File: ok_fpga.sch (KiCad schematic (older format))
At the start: 39 parts, among them J12 Conn_Coaxial, J13 QWIIC_CONNECTOR-1MM, J14 Conn_Coaxial, J22 Conn_02x10_Counter_Clockwise, J23 Conn_02x10_Counter_Clockwise, U15 PCA9306, U16 NLSX3018DTR2G, U18 TXS0108EPW, U20 TXS0108EPW, U24 TCA9555, U25 TCA9555

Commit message: moved DCO 7960 signals to dedicated input clock routes
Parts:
- J12, J14: footprint (none) -> covg-kicad:BU-SMA-G; Manf# (none) -> WM26450
- J23: symbol Connector_Generic:Conn_02x05_Counter_Clockwise -> Connector_Generic:Conn_02x05_Odd_Even
- gave numbers to parts that had none: 18
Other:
- note added: "11 is a clock in"
- note added: "12 is a clock in"
- note added: "13 is a clock in"
- note added: "14 is a clock in"
- note removed: "Do a check of skew matching between DCO and D \nfor high-speed ADC"
- moved on the sheet: U24, U25

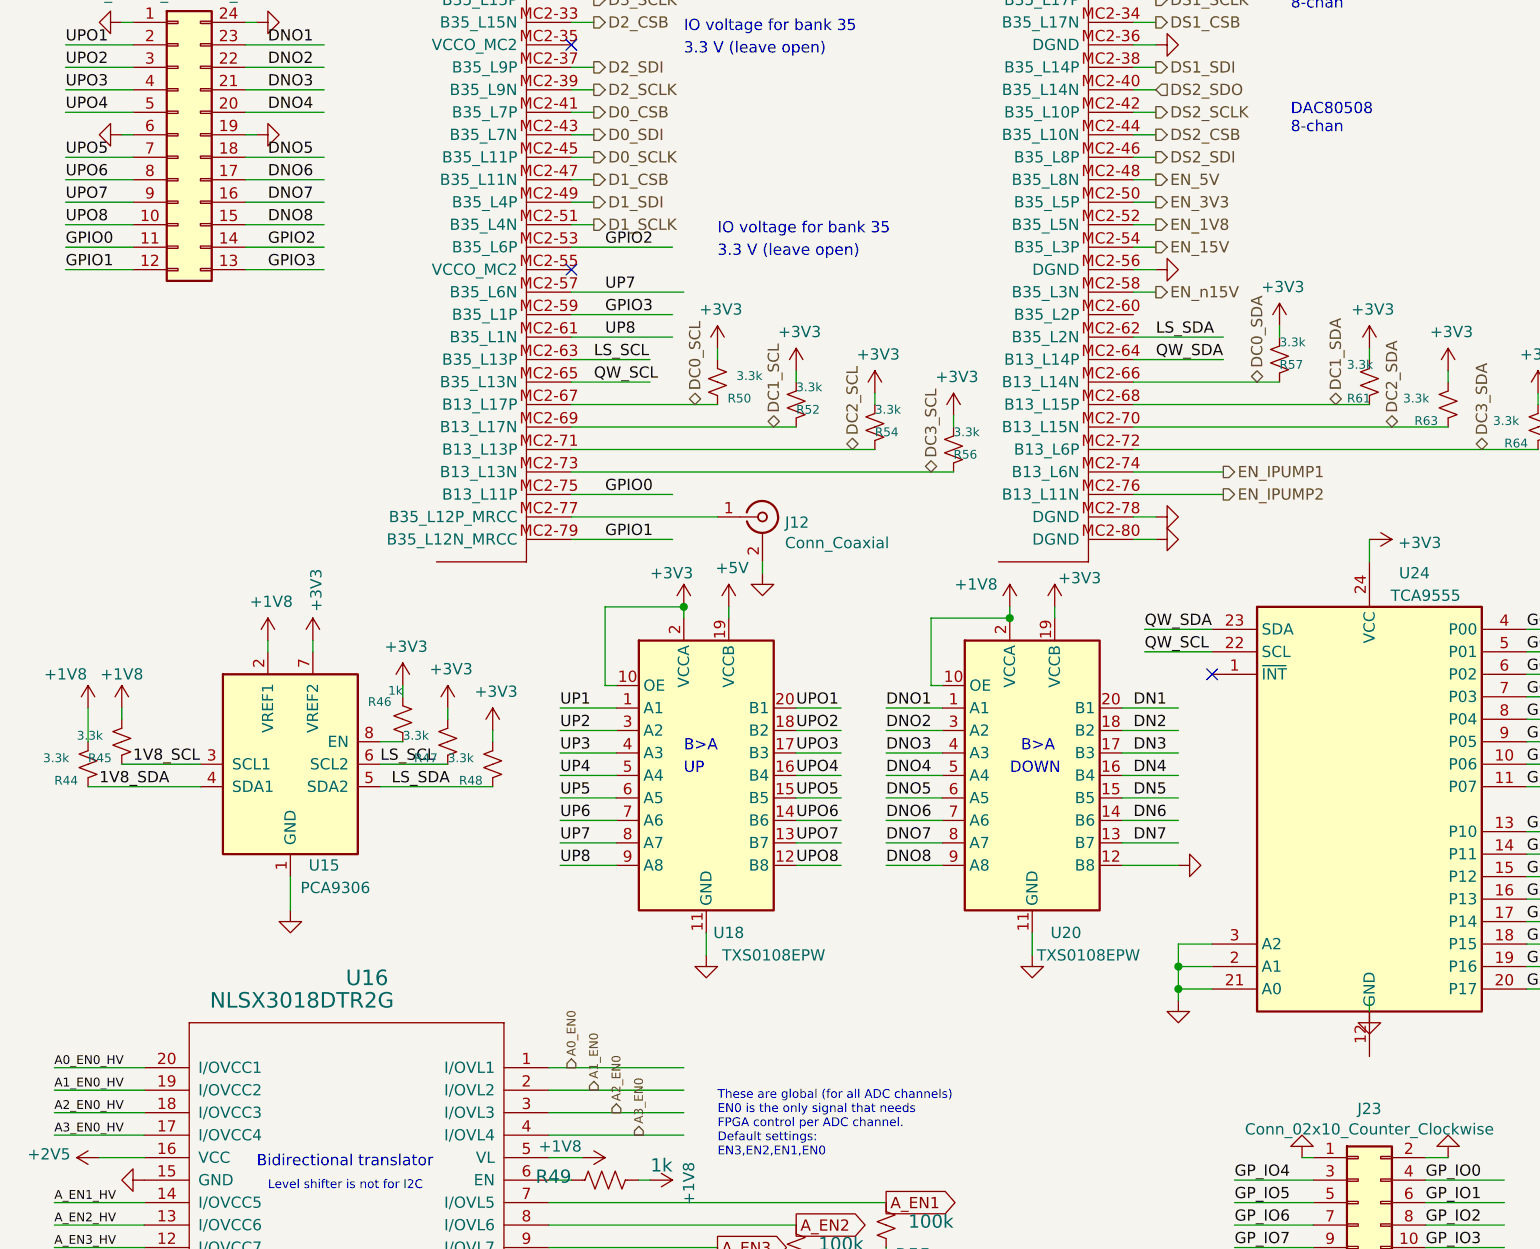
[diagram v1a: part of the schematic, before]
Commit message: added Unique ID chip
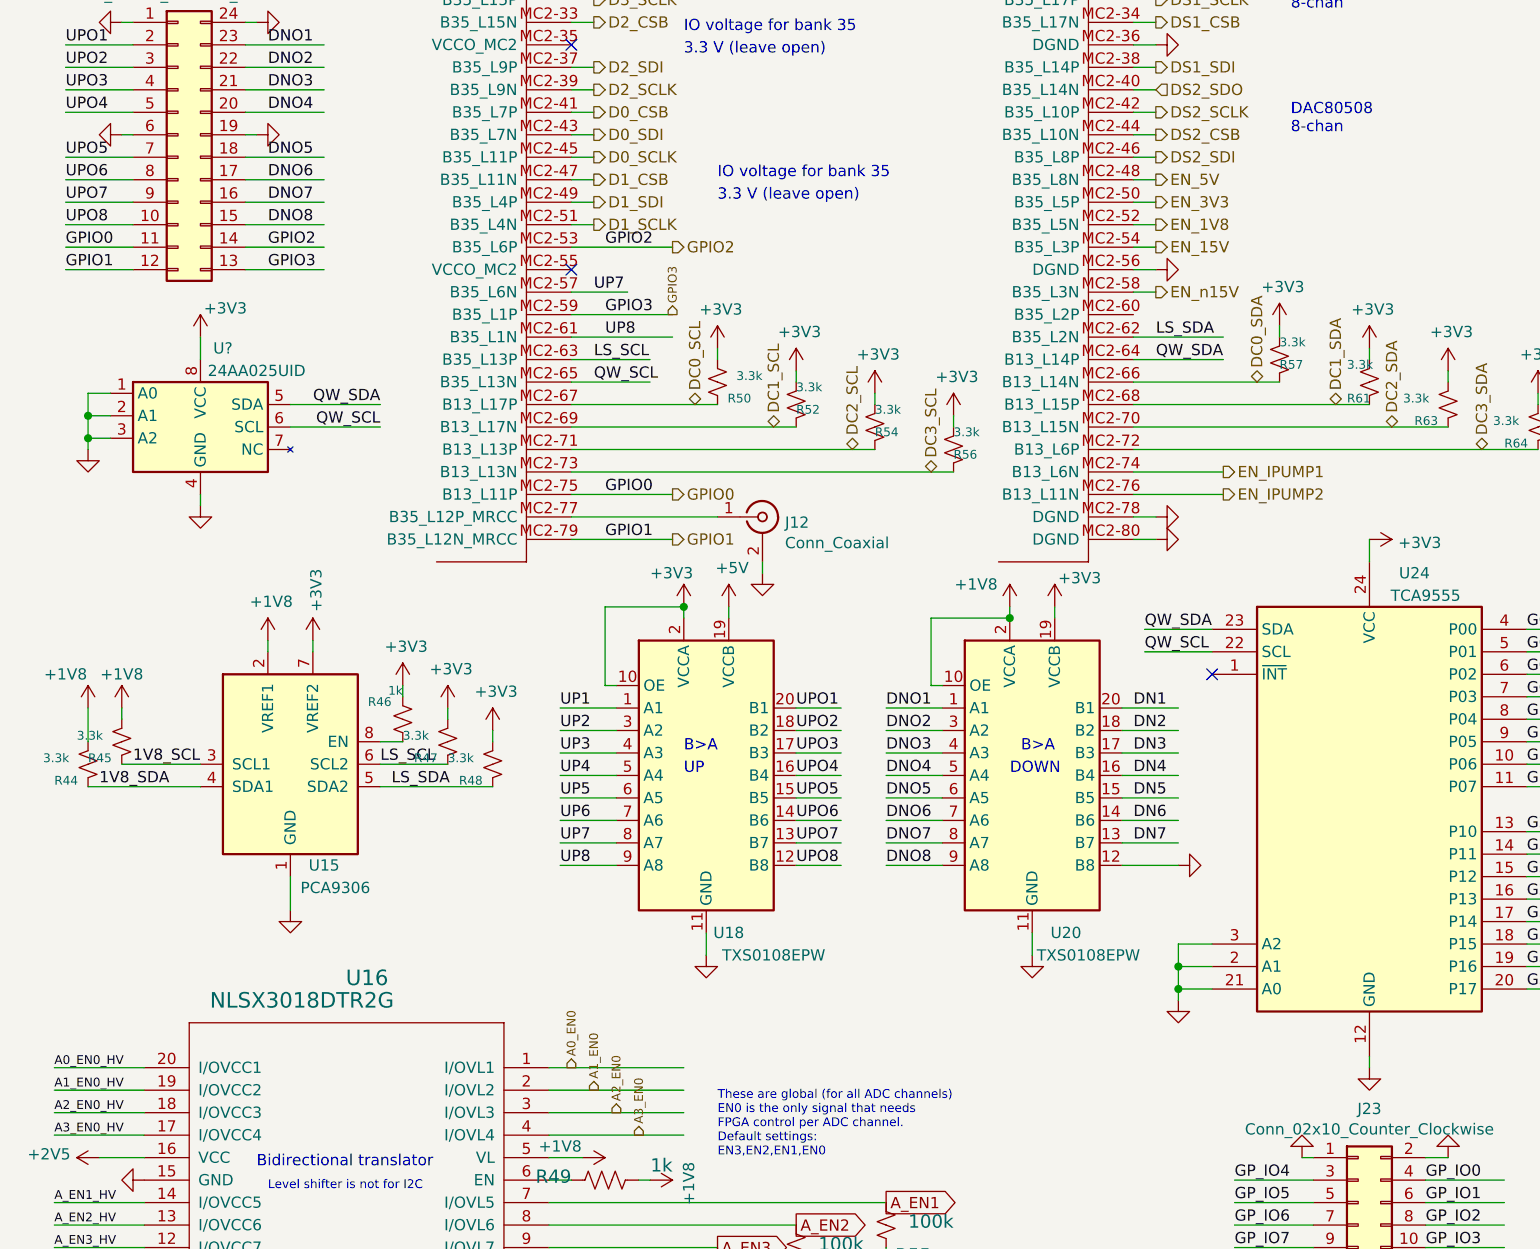
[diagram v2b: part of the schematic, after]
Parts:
- added U?: 24AA025UID, Package_SO:SOIC-8_3.9x4.9mm_P1.27mm, symbol covg-kicad:24AA025UID
- OK1: footprint covg-kicad:OPALKELLY_XEM6010 -> covg-kicad:OPALKELLY_XEM7310
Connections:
- wire segments 344 -> 354
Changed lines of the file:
@@
 F 0 "OK1" H 2700 4610 70  0000 R BNN
 F 1 "OPALKELLY_XEM6310" H 2500 2600 50  0001 C CNN
-F 2 "covg-kicad:OPALKELLY_XEM6010" H 2500 2600 50  0001 C CNN
+F 2 "covg-kicad:OPALKELLY_XEM7310" H 2500 2600 50  0001 C CNN
 F 3 "" H 2500 2600 50  0001 C CNN
 F 4 "BTE-040-02-F-D-A" H 2700 4710 50  0001 C CNN "Manf#"
@@
 F 0 "OK1" H 8000 4610 70  0000 R BNN
 F 1 "OPALKELLY_XEM6310" H 7800 2600 50  0001 C CNN
-F 2 "covg-kicad:OPALKELLY_XEM6010" H 7800 2600 50  0001 C CNN
+F 2 "covg-kicad:OPALKELLY_XEM7310" H 7800 2600 50  0001 C CNN
 F 3 "" H 7800 2600 50  0001 C CNN
 F 4 "BTE-040-02-F-D-A" H 8000 4710 50  0001 C CNN "Manf#"
@@
 F 0 "OK1" H 10700 4610 70  0000 R BNN
 F 1 "OPALKELLY_XEM6310" H 10500 2600 50  0001 C CNN
-F 2 "covg-kicad:OPALKELLY_XEM6010" H 10500 2600 50  0001 C CNN
+F 2 "covg-kicad:OPALKELLY_XEM7310" H 10500 2600 50  0001 C CNN
 F 3 "" H 10500 2600 50  0001 C CNN
 F 4 "BTE-040-02-F-D-A" H 10700 4710 50  0001 C CNN "Manf#"
@@
 F 0 "OK1" H 5200 4610 70  0000 R BNN
 F 1 "OPALKELLY_XEM6310" H 5000 2600 50  0001 C CNN
-F 2 "covg-kicad:OPALKELLY_XEM6010" H 5000 2600 50  0001 C CNN
+F 2 "covg-kicad:OPALKELLY_XEM7310" H 5000 2600 50  0001 C CNN
 F 3 "" H 5000 2600 50  0001 C CNN
 F 4 "BTE-040-02-F-D-A" H 5200 4710 50  0001 C CNN "Manf#"
@@
 L power:GND #GND0150
 U 1 1 62BA3427
-P 6450 6700
-F 0 "#GND0150" H 6450 6700 50  0001 C CNN
-F 1 "GND" H 6350 6600 59  0001 L BNN
-F 2 "" H 6450 6700 50  0001 C CNN
-F 3 "" H 6450 6700 50  0001 C CNN
-	1    6450 6700
+P 6450 6950
+F 0 "#GND0150" H 6450 6950 50  0001 C CNN
+F 1 "GND" H 6350 6850 59  0001 L BNN
+F 2 "" H 6450 6950 50  0001 C CNN
+F 3 "" H 6450 6950 50  0001 C CNN
+	1    6450 6950
 	1    0    0    -1
 $EndComp
@@
 Text Notes 10250 2350 3    50   ~ 0
 IO voltage for bank 34
-Text Notes 3550 3250 0    50   ~ 0
+Text Notes 3550 3000 0    50   ~ 0
 IO voltage for bank 35
 Text Notes 3400 2350 0    50   ~ 0
@@
 Text Notes 11150 5700 0    39   ~ 0
 SparkFun qwiic connector\nSM04B-SRSS-TB\n3.3 V VCC
-Text Label 3050 3500 0    50   ~ 0
+Text Label 3000 3500 0    50   ~ 0
 UP7
 Text Label 3000 3900 0    50   ~ 0
@@
 Text Notes 3300 1200 0    50   ~ 0
 SYS_CLK not special \nother than name
-Text Notes 3550 3350 0    50   ~ 0
+Text Notes 3550 3100 0    50   ~ 0
 3.3 V (leave open)
 Text Label 5450 5000 0    50   ~ 0
@@
 	600  6950 1000 6950
 Wire Wire Line
-	2900 3500 3400 3500
+	2900 3500 3150 3500
 Wire Wire Line
 	1750 5100 1750 5050
@@
 Wire Wire Line
 	6450 4600 6450 4700
-Wire Wire Line
-	6450 6700 6450 6650
 Wire Wire Line
 	5750 6400 5600 6400
@@
 Wire Wire Line
 	3600 4900 3600 4950
+Wire Wire Line
+	6450 6950 6450 6900
+Text HLabel 3350 4400 2    50   Output ~ 0
+GPIO0
+Text HLabel 3350 4600 2    50   Output ~ 0
+GPIO1
+Text HLabel 3350 3300 2    50   Output ~ 0
+GPIO2
+Text HLabel 3350 3600 1    39   Output ~ 0
+GPIO3
+$Comp
+L covg-kicad:24AA025UID U?
+U 1 1 60CE7EFE
+P 1250 4100
+F 0 "U?" H 1350 4450 50  0000 C CNN
+F 1 "24AA025UID" H 1500 4350 50  0000 C CNN
+F 2 "Package_SO:SOIC-8_3.9x4.9mm_P1.27mm" H 1250 4100 50  0001 C CNN
+F 3 "https://ww1.microchip.com/downloads/en/DeviceDoc/20005202A.pdf" H 1250 4100 50  0001 C CNN
+	1    1250 4100
+	1    0    0    -1
+$EndComp
+$Comp
+L power:+3V3 #PWR?
+U 1 1 60CE899F
+P 1250 3700
+F 0 "#PWR?" H 1250 3550 50  0001 C CNN
+F 1 "+3V3" H 1265 3828 50  0000 L CNN
+F 2 "" H 1250 3700 50  0001 C CNN
+F 3 "" H 1250 3700 50  0001 C CNN
+	1    1250 3700
+	1    0    0    -1
+$EndComp
+Wire Wire Line
+	1250 3700 1250 3800
+$Comp
+L power:GND #GND?
+U 1 1 60D1BC8F
+P 1250 4450
+F 0 "#GND?" H 1250 4450 50  0001 C CNN
+F 1 "GND" H 1150 4350 59  0001 L BNN
+F 2 "" H 1250 4450 50  0001 C CNN
+F 3 "" H 1250 4450 50  0001 C CNN
+	1    1250 4450
+	1    0    0    -1
+$EndComp
+Wire Wire Line
+	1250 4450 1250 4400
+Text Label 2050 4100 2    50   ~ 0
+QW_SCL
+Text Label 2050 4000 2    50   ~ 0
+QW_SDA
+Wire Wire Line
+	2050 4100 1650 4100
+Wire Wire Line
+	1650 4000 2050 4000
+Wire Wire Line
+	850  3950 750  3950
+Wire Wire Line
+	750  3950 750  4050
+Wire Wire Line
+	750  4150 850  4150
+Wire Wire Line
+	850  4050 750  4050
+Connection ~ 750  4050
+Wire Wire Line
+	750  4050 750  4150
+$Comp
+L power:GND #GND?
+U 1 1 60E1D852
+P 750 4200
+F 0 "#GND?" H 750 4200 50  0001 C CNN
+F 1 "GND" H 650 4100 59  0001 L BNN
+F 2 "" H 750 4200 50  0001 C CNN
+F 3 "" H 750 4200 50  0001 C CNN
+	1    750  4200
+	1    0    0    -1
+$EndComp
+Wire Wire Line
+	750  4200 750  4150
 Wire Bus Line
 	7600 5500 7600 5800
@@
 Wire Bus Line
 	9100 2250 9100 2700
+Connection ~ 750  4150
 $EndSCHEMATC

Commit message: layout cleanup; removed custom footrpints
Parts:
- added J24: Conn_01x02_Counter_Clockwise, Connector_PinHeader_2.54mm:PinHeader_1x02_P2.54mm_Vertical_SMD_Pin1Left, symbol Connector_Generic:Conn_01x02
- added R286: DNI, Resistor_SMD:R_0603_1608Metric, symbol Device:R_US
- added TP1, TP2, TP3, TP4, TP5, TP6, TP7: TestPoint, TestPoint:TestPoint_THTPad_1.5x1.5mm_Drill0.7mm, symbol Connector:TestPoint
- J22: footprint (none) -> Connector_PinHeader_2.54mm:PinHeader_2x10_P2.54mm_Horizontal; symbol Connector_Generic:Conn_02x12_Counter_Clockwise -> Connector_Generic:Conn_02x10_Counter_Clockwise
- J23: value Conn_02x10_Counter_Clockwise -> Conn_02x05_Odd_Even; footprint (none) -> Connector_PinHeader_2.54mm:PinHeader_2x05_P2.54mm_Horizontal
- gave numbers to parts that had none: 1
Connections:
- net labels added: DN0, DNO0, GP_LVDS_0N, GP_LVDS_0P, GP_LVDS_1N, GP_LVDS_1P, GP_LVDS_2N, GP_LVDS_2P, GP_LVDS_3N, GP_LVDS_3P, UP0, UPO0, XADC_VN, XADC_VP
- net labels removed: DN6, DN7, DNO6, DNO7, DNO8, GP_IO0, GP_IO1, GP_IO2, GP_IO3, GP_IO4, GP_IO5, GP_IO6, GP_IO7, UP6, UP7, UP8, UPO6, UPO7, UPO8
- wire segments 354 -> 353
- no-connect marks 13 -> 21
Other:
- note added: "DAC gain \ncontrol"
- note added: "FPGA power: standard “canon-style” 2.1mm / 5.5mm jack. The outer ring is connected to DGND. The center pin is connected to +VDC."
- note added: "MRCC - multi-region clock capable"
- note added: "VCCBATT is the battery backup supply for the FPGA’s internal volatile memory that stores the key for the AES decryptor (not needed)"
- note removed: "Ok for 2.5 V \nto TMUX since \nref to Gnd"
- note removed: "SYS_CLK not special \nother than name"
- note removed: "What is VCCBATT?"
- moved on the sheet: J13, R70, R71

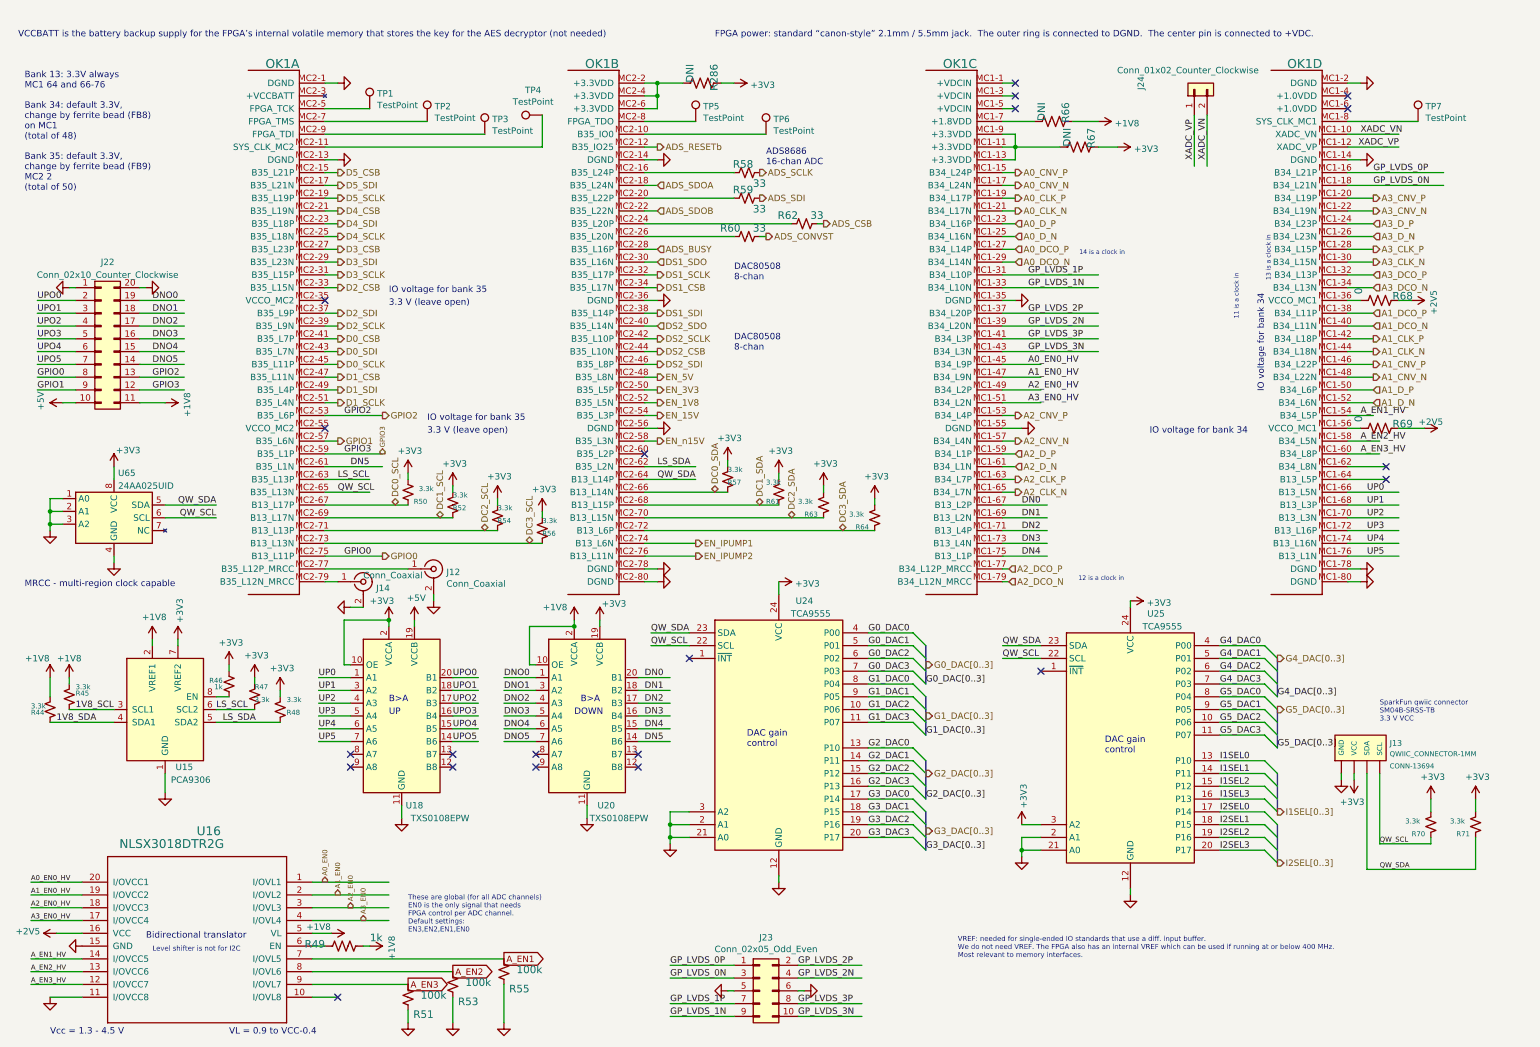
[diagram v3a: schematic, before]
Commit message: updates of DAC part placement
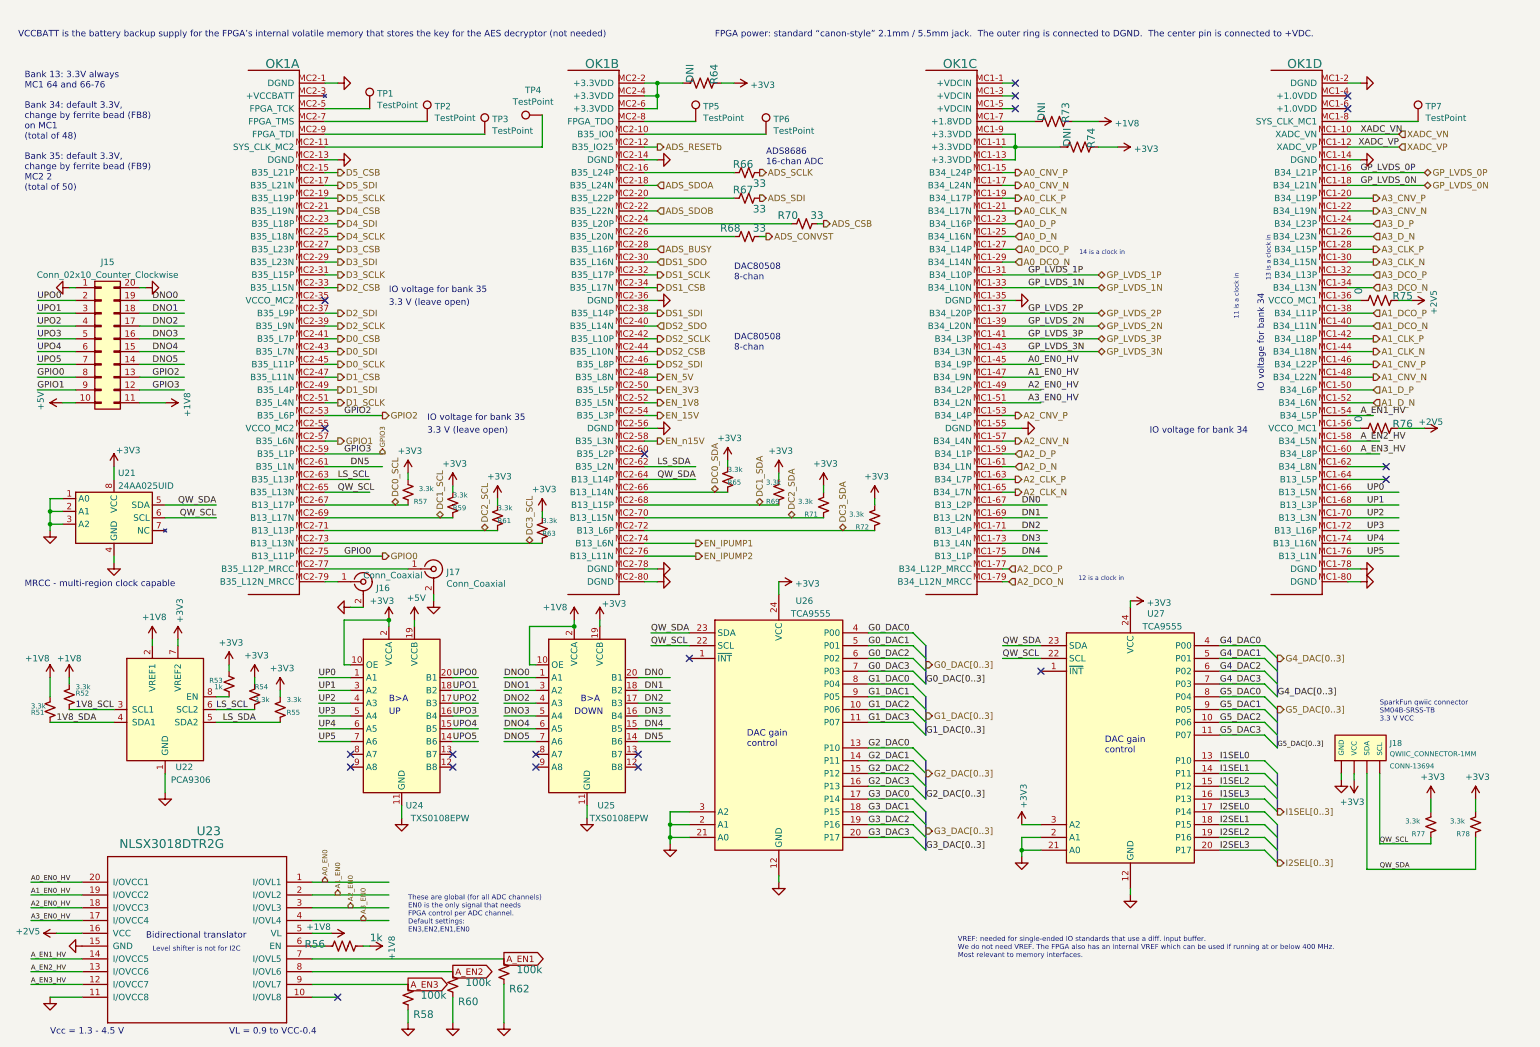
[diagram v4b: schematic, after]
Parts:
- removed J23: Conn_02x05_Odd_Even, Connector_PinHeader_2.54mm:PinHeader_2x05_P2.54mm_Horizontal, symbol Connector_Generic:Conn_02x05_Odd_Even
- removed J24: Conn_01x02_Counter_Clockwise, Connector_PinHeader_2.54mm:PinHeader_1x02_P2.54mm_Vertical_SMD_Pin1Left, symbol Connector_Generic:Conn_01x02
- renumbered J22 to J15, J14 to J16, J12 to J17, J13 to J18, R44 to R51, R45 to R52, R46 to R53, R47 to R54, R48 to R55, R49 to R56, R50 to R57, R51 to R58, R52 to R59, R53 to R60, R54 to R61, R55 to R62, R56 to R63, R286 to R64, R57 to R65, R58 to R66, R59 to R67, R60 to R68, R61 to R69, R62 to R70, R63 to R71, R64 to R72, R66 to R73, R67 to R74, R68 to R75, R69 to R76, R70 to R77, R71 to R78, U65 to U21, U15 to U22, U16 to U23, U18 to U24, U20 to U25, U24 to U26, U25 to U27
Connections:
- wire segments 353 -> 341

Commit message: updated component placement
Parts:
- added R286, R289: DNI, Resistor_SMD:R_0603_1608Metric, symbol Device:R_Small_US
- added R287, R288: 49.9, Resistor_SMD:R_0603_1608Metric, symbol Device:R_Small_US
- J15: value Conn_02x10_Counter_Clockwise -> Conn_02x12_Counter_Clockwise; footprint Connector_PinHeader_2.54mm:PinHeader_2x10_P2.54mm_Horizontal -> Connector_PinHeader_2.00mm:PinHeader_2x12_P2.00mm_Horizontal; symbol Connector_Generic:Conn_02x10_Counter_Clockwise -> Connector_Generic:Conn_02x12_Counter_Clockwise
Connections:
- wire segments 341 -> 352
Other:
- moved on the sheet: J16, J17, R51, R52, R53, R54, R55, U21, U22
